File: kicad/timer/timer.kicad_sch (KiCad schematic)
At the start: 13 parts, among them SW1 SW_Push, U1 ATmega328P-P, Y1 Crystal

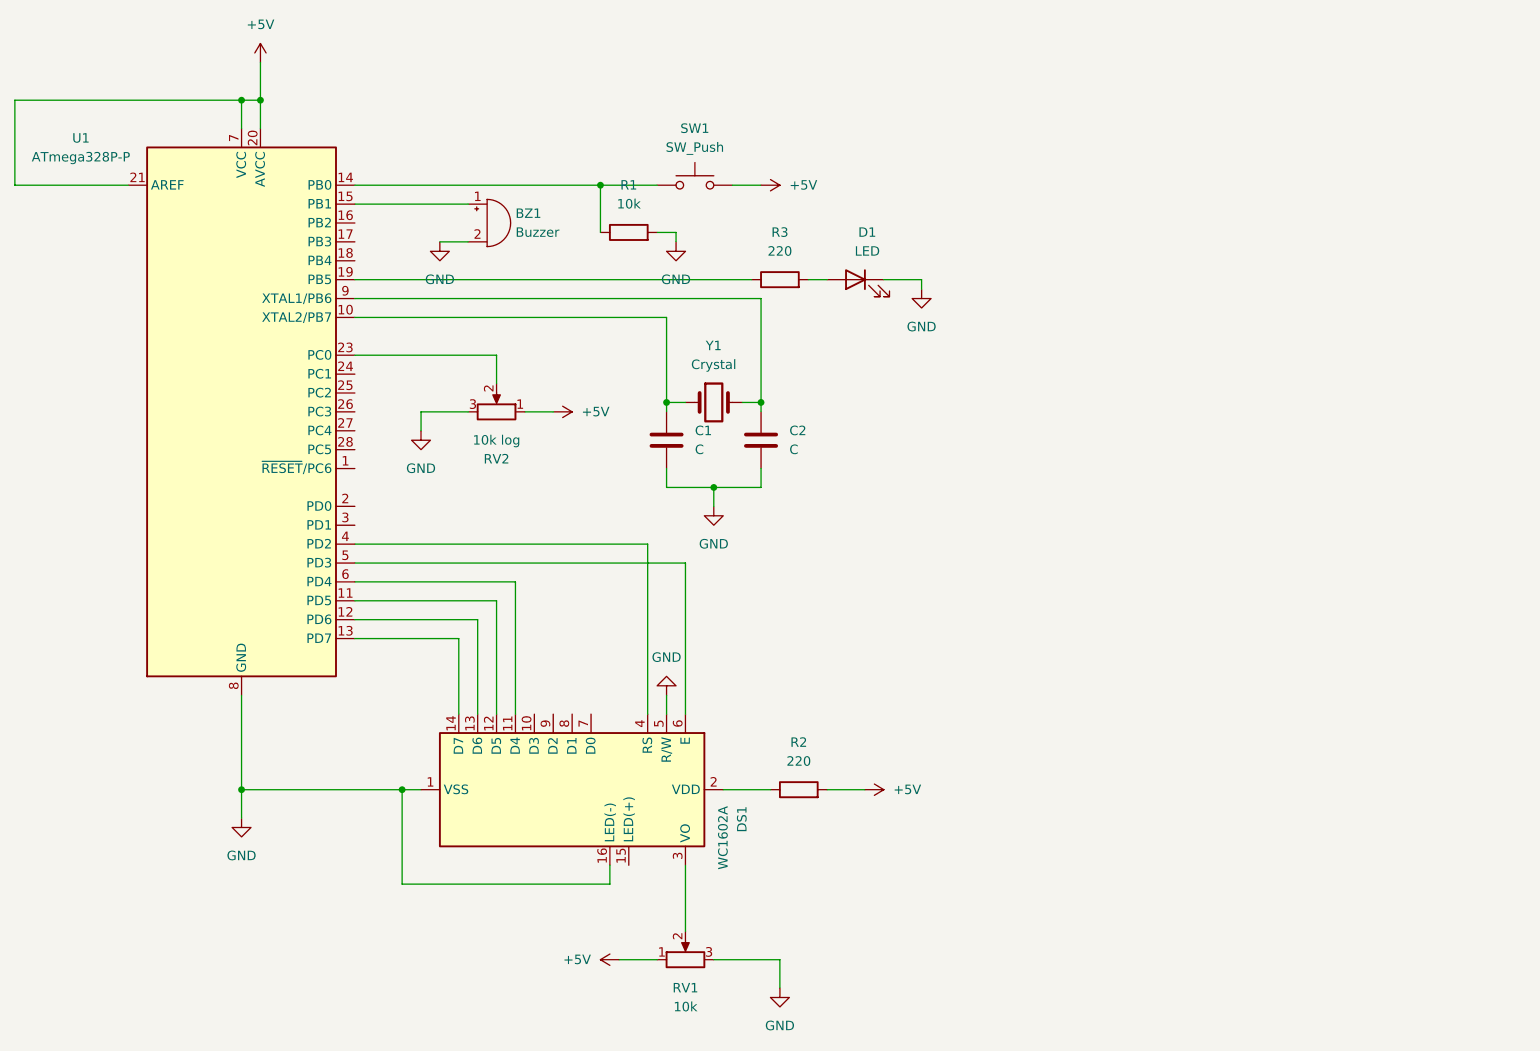
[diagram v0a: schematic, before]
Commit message: Add voltage regulator
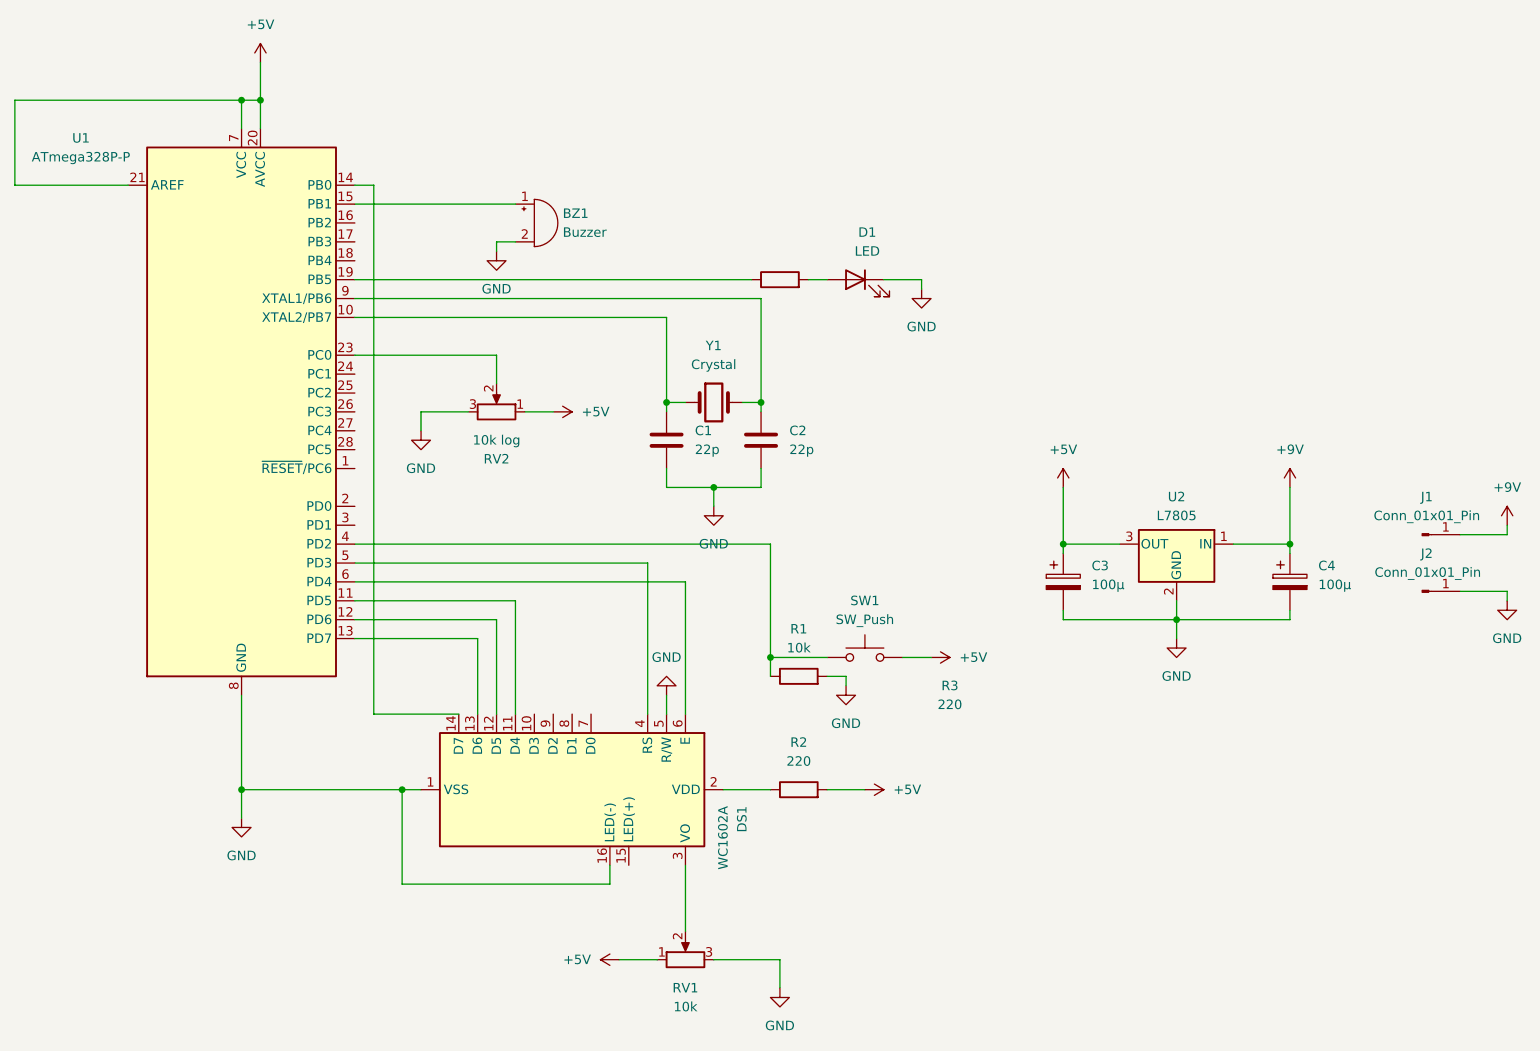
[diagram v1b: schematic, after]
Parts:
- added C3, C4: 100µ, Capacitor_THT:CP_Radial_D6.3mm_P2.50mm, symbol Device:C_Polarized
- added J1, J2: Conn_01x01_Pin, Connector_Wire:SolderWire-0.1sqmm_1x01_D0.4mm_OD1mm, symbol Connector:Conn_01x01_Pin
- added U2: L7805, Package_TO_SOT_THT:TO-220-3_Vertical, symbol Regulator_Linear:L7805
- C1, C2: value C -> 22p
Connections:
- net +5V: now also C3.1, U2.3 (OUT)
- net GND: now also C3.2, C4.2, J2.1 (Pin_1), U2.2 (GND)
- net at R1.1, SW1.1: now also U1.4 (PD2); no longer U1.14 (PB0)
- net at U1.11 (PD5): now also DS1.11 (D4); no longer DS1.12 (D5)
- net at U1.12 (PD6): now also DS1.12 (D5); no longer DS1.13 (D6)
- net at U1.13 (PD7): now also DS1.13 (D6); no longer DS1.14 (D7)
- net at DS1.4 (RS): now also U1.5 (PD3); no longer U1.4 (PD2)
- net at DS1.6 (E): now also U1.6 (PD4); no longer U1.5 (PD3)
- new net: DS1.14 (D7), U1.14 (PB0)
- new net +9V: C4.1, J1.1 (Pin_1), U2.1 (IN)
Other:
- moved on the sheet: BZ1, R1, SW1

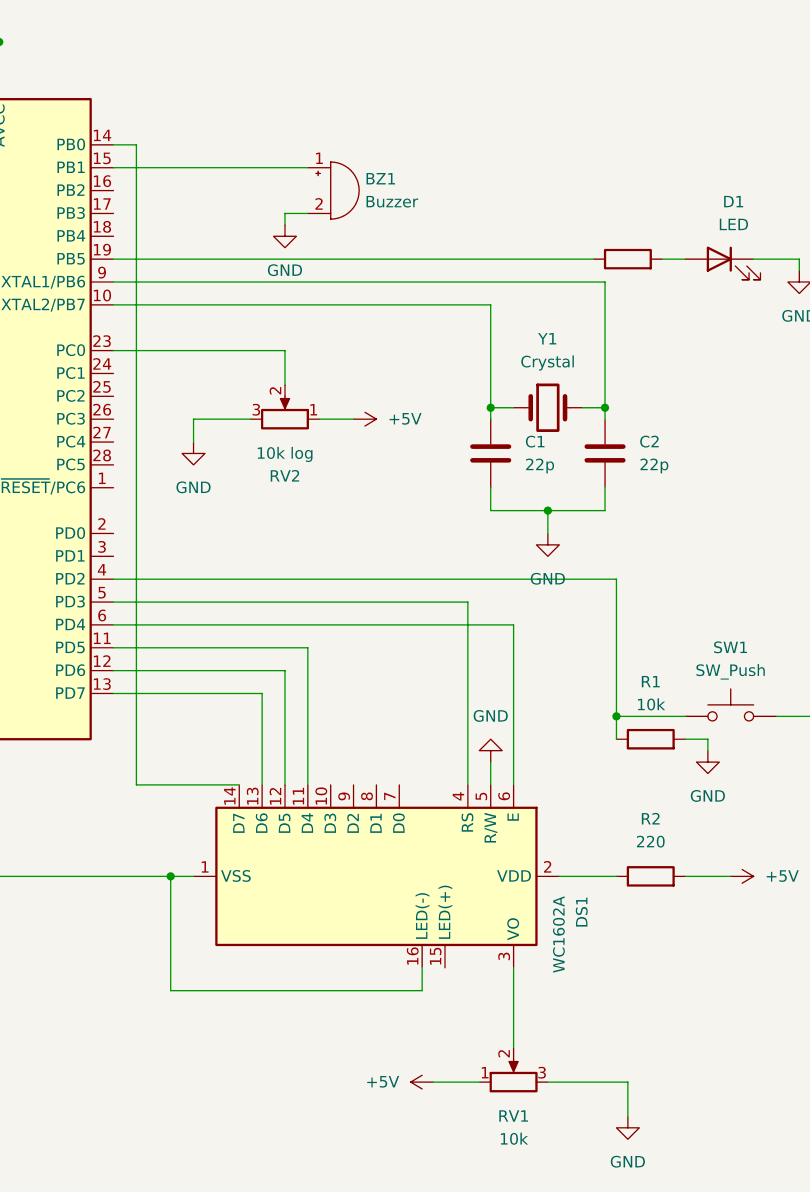
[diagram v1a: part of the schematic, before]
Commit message: Add missing connection of LCD/LED+ to +5V
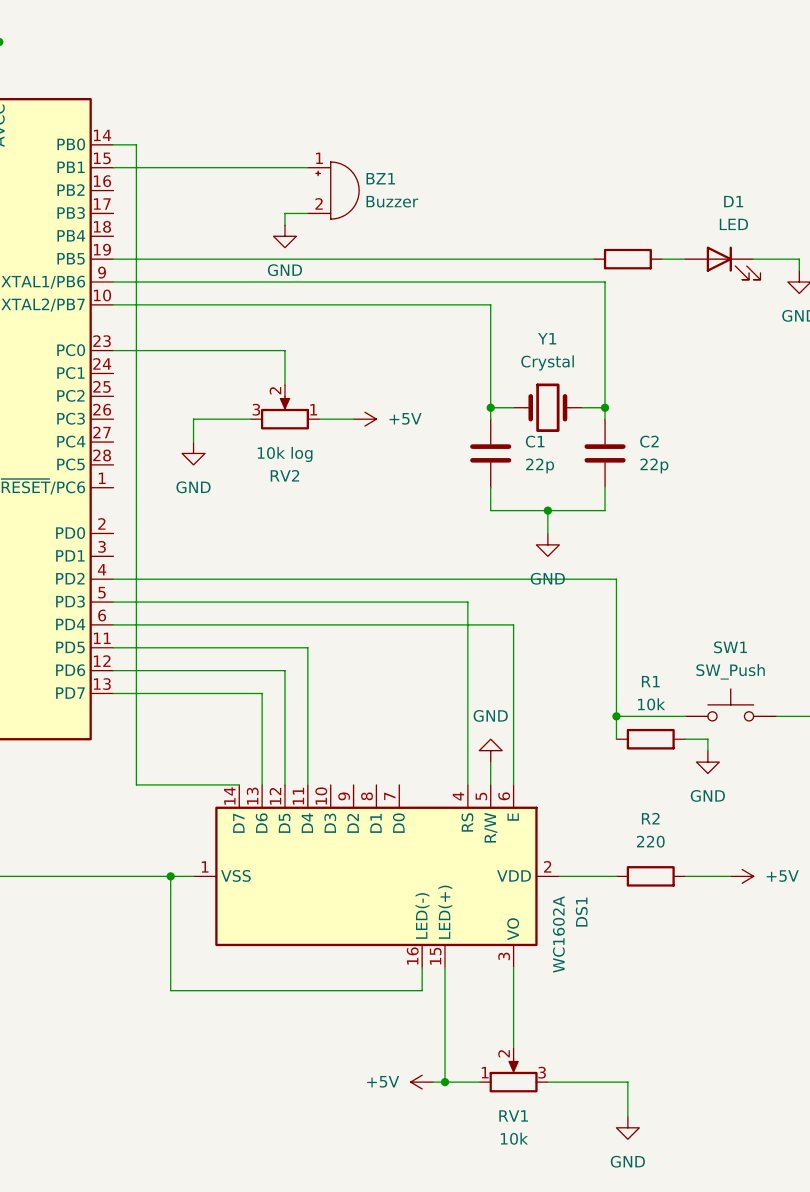
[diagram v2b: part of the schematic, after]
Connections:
- net +5V: now also DS1.15 (LED(+))
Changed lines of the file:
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@@
 (kicad_sch
-	(version 20231120)
+	(version 20250114)
 	(generator "eeschema")
-	(generator_version "8.0")
+	(generator_version "9.0")
 	(paper "A4")
 	(junction
@@
 	)
 	(junction
+		(at 142.24 148.59)
+		(diameter 0)
+		(color 0 0 0 0)
+	)
+	(junction
 		(at 161.29 107.95)
 		(diameter 0)
@@
 	(wire
 		(pts
+			(xy 142.24 148.59) (xy 140.97 148.59)
+		)
+		(stroke
+			(width 0)
+			(type default)
+		)
+	)
+	(wire
+		(pts
 			(xy 114.3 74.93) (xy 114.3 77.47)
 		)
@@
 	(wire
 		(pts
-			(xy 146.05 148.59) (xy 140.97 148.59)
+			(xy 146.05 148.59) (xy 142.24 148.59)
 		)
 		(stroke
@@
 	(wire
 		(pts
+			(xy 142.24 135.89) (xy 142.24 148.59)
+		)
+		(stroke
+			(width 0)
+			(type default)
+		)
+	)
+	(wire
+		(pts
 			(xy 59.69 44.45) (xy 74.93 44.45)
 		)
@@
 		)
 	)
+	(embedded_fonts no)
 )
